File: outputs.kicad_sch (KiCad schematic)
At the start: 38 parts, among them IC1 TLE9201SG, Q1 ISL9V3040D3ST, Q2 ISL9V3040D3ST, Q3 DMN6040SK3-13, Q4 DMN6040SK3-13, U2 VNLD5160TR-E, U3 VNLD5160TR-E, U4 VNLD5160TR-E, U7 VNLD5160TR-E, U8 VNLD5160TR-E

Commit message: ACR mosfet
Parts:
- removed U3: VNLD5160TR-E, VNLD5160TR-E:SO_160TR-E_STM, symbol VNLD5160TR-E:VNLD5160TR-E
- added Q5: BUK9K52-60E,115, BUK9K52-60E:BUK7K6R840E115, symbol BUK9K52-60E_115:BUK9K52-60E,115
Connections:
- net ACR_1: now also Q5.7 (D1_1), Q5.8 (D1_2), Q5.9 (D1_3)
- net ACR_2: now also Q5.10 (D2_3), Q5.5 (D2_1), Q5.6 (D2_2); no longer U2.6 (DRAIN2)
- net GND: now also Q5.1 (S1), Q5.3 (S2)
- net INJ_1: now also U2.8 (DRAIN1)
- net INJ_2: now also U2.6 (DRAIN2); no longer U2.8 (DRAIN1)
- net MCU_ACR1: now also Q5.2 (G1)
- net MCU_ACR2: now also Q5.4 (G2); no longer U2.3 (IN2/VSUPPLY2)
- net MCU_INJ1: now also R3.1, U2.1 (IN1/VSUPPLY1); no longer R6.1
- net MCU_INJ2: now also R6.1, U2.3 (IN2/VSUPPLY2); no longer R3.1, U2.1 (IN1/VSUPPLY1)
- no-connect marks 11 -> 9
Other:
- note added: "ACR"
- note added: "ACR use same as Harley BUK9K52-60E"
- note added: "CCFC: Harley uses 2N06L35 TODO!"
- note added: "INJECTORS"
- note removed: "INJECTORS & ACR"

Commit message: some documentation and etc_dir added
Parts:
- R14: value R_Small -> 4.7K
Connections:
- net ETC_DIS: now reaches IC1.11 (DIS), R14.1
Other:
- note added: "COOLANT FAN PULLS AROUND 4A WHEN CONSTANT 100%, INITIALLY PULLING UP TO 8A FOR GETTING SPINNING HARLEY USES: HUFA76429D3 POSSIBLE: https://www.digikey.de/de/products/detail/onsemi/HUF76629D3ST/4553106 AND: https://www.digikey.de/de/products/detail/diodes-incorporated/DMN6040SK3-13/8545933 Weytronik: https://www.digikey.de/de/products/detail/vishay-siliconix/SISS54DN-T1-GE3/14004251?s=N4IgTCBcDaIM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"
- note added: "H2OS Heaters are PWM Controlled and max out at about 0.9 Amps at room temperature, then reducing with heat coming. VNLD5160TR-E should work. Will test"
- note added: "Harley Uses: https://www.mouser.de/ProductDetail/onsemi/FGB3040G2-F085C?qs=2WXlatMagcHzMRj1hscbYQ%3D%3D ISL9V3040D3ST should work though"
- note added: "INJECTORS MEASURED TO TAKE MAX 1A EACH WHEN OPEN VNLD5160TR-E should be fine"
- note added: "TODO: PURGE AND VVT SOLENOIDS NOT MEASURED YET AT ALL"
- note removed: "COOLANT FAN PULLS AROUND 4A WHEN CONSTANT 100%, INITIALLY PULLING UP TO 8A FOR GETTING SPINNING HARLEY USES: HUFA76429D3 POSSIBLE: https://www.digikey.de/de/products/detail/onsemi/HUF76629D3ST/4553106 AND: https://www.digikey.de/de/products/detail/diodes-incorporated/DMN6040SK3-13/8545933"
- note removed: "H2OS Heaters are PWM Controlled and max out at about 0.9 Amps at room temperature, then reducing with coming heat"
- note removed: "Harley Uses: https://www.mouser.de/ProductDetail/onsemi/FGB3040G2-F085C?qs=2WXlatMagcHzMRj1hscbYQ%3D%3D"
- note removed: "INJECTORS MEASURED TO TAKE MAX 1A EACH WHEN OPEN"
- moved on the sheet: C10, C11, C12, C13, C14, C15, C16, C17, C5, C6, C7, C8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

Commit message: update main connector footprint
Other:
- note added: "H2OS Heaters are PWM Controlled and max out at about 0.9 Amps at room temperature, then reducing with heat coming. VNLD5160TR-E should work. Will test HD uses https://www.vishay.com/docs/71506/sq4946aey.pdf"
- note added: "INJECTORS MEASURED TO TAKE MAX 1A EACH WHEN OPEN VNLD5160TR-E should be fine HARLEY uses 2N06L35"
- note removed: "H2OS Heaters are PWM Controlled and max out at about 0.9 Amps at room temperature, then reducing with heat coming. VNLD5160TR-E should work. Will test"
- note removed: "INJECTORS MEASURED TO TAKE MAX 1A EACH WHEN OPEN VNLD5160TR-E should be fine"
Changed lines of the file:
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@@
 			(font
 				(size 2 2)
-				(thickness 0.6)
-				(bold yes)
+				(thickness 0.25)
 				(color 43 255 15 1)
 			)
@@
 		)
 	)
-	(text "INJECTORS MEASURED TO TAKE MAX 1A EACH WHEN OPEN\nVNLD5160TR-E should be fine"
+	(text "INJECTORS MEASURED TO TAKE MAX 1A EACH WHEN OPEN\nVNLD5160TR-E should be fine\nHARLEY uses 2N06L35"
 		(exclude_from_sim no)
 		(at 103.124 61.722 0)
@@
 		)
 	)
-	(text "H2OS Heaters are PWM Controlled and max out at about 0.9 Amps\nat room temperature, then reducing with heat coming.\nVNLD5160TR-E should work. Will test"
+	(text "H2OS Heaters are PWM Controlled and max out at about 0.9 Amps\nat room temperature, then reducing with heat coming.\nVNLD5160TR-E should work. Will test\nHD uses https://www.vishay.com/docs/71506/sq4946aey.pdf"
 		(exclude_from_sim no)
 		(at 306.578 156.21 0)
@@
 				(thickness 0.6)
 				(bold yes)
+				(color 255 238 0 1)
+			)
+		)
+	)
+	(text "Harley Uses:\nhttps://www.mouser.de/ProductDetail/onsemi/FGB3040G2-F085C?qs=2WXlatMagcHzMRj1hscbYQ%3D%3D\nISL9V3040D3ST should work though"
+		(exclude_from_sim no)
+		(at 98.806 278.13 0)
+		(effects
+			(font
+				(size 2 2)
+				(thickness 0.25)
 				(color 43 255 15 1)
 			)
@@
 			(font
 				(size 2 2)
-				(thickness 0.6)
-				(bold yes)
+				(thickness 0.25)
 				(color 43 255 15 1)
 			)
@@
 	(text "CCFC & HO2HTR"
 		(exclude_from_sim no)
-		(at 307.34 217.424 0)
+		(at 308.102 219.71 0)
 		(effects
 			(font
@@
 	(text "H2OS Heaters"
 		(exclude_from_sim no)
-		(at 308.61 167.894 0)
+		(at 307.34 171.704 0)
 		(effects
 			(font
@@
 	(text "CCFC: Harley uses 2N06L35 TODO!"
 		(exclude_from_sim no)
-		(at 306.07 210.82 0)
+		(at 306.832 213.106 0)
 		(effects
 			(font
@@
 				(thickness 0.6)
 				(bold yes)
-				(color 43 255 15 1)
+				(color 255 238 0 1)
 			)
 		)

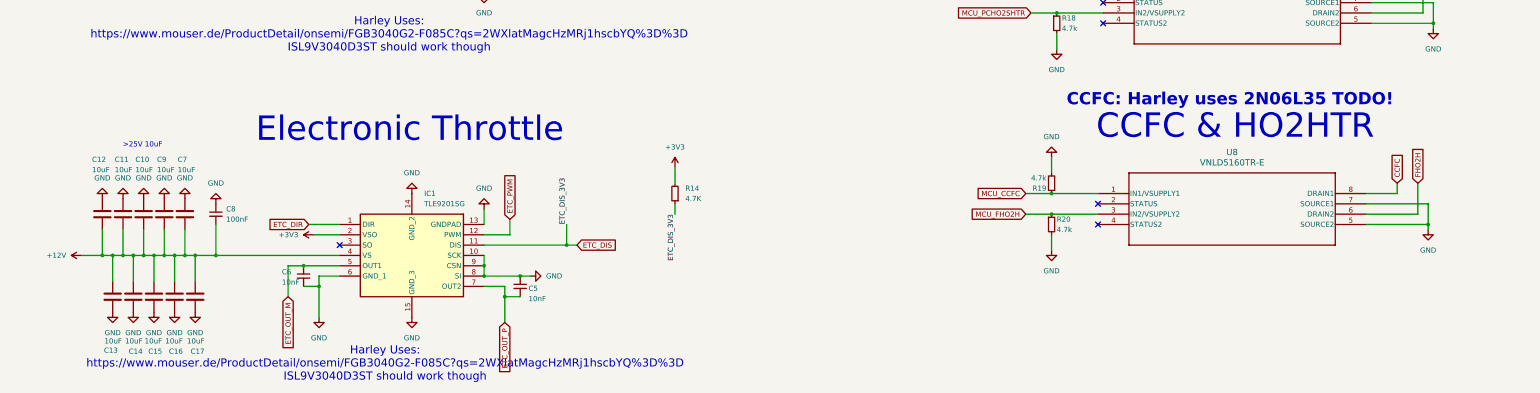
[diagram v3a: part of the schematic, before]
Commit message: ccfc mosfet and power changes
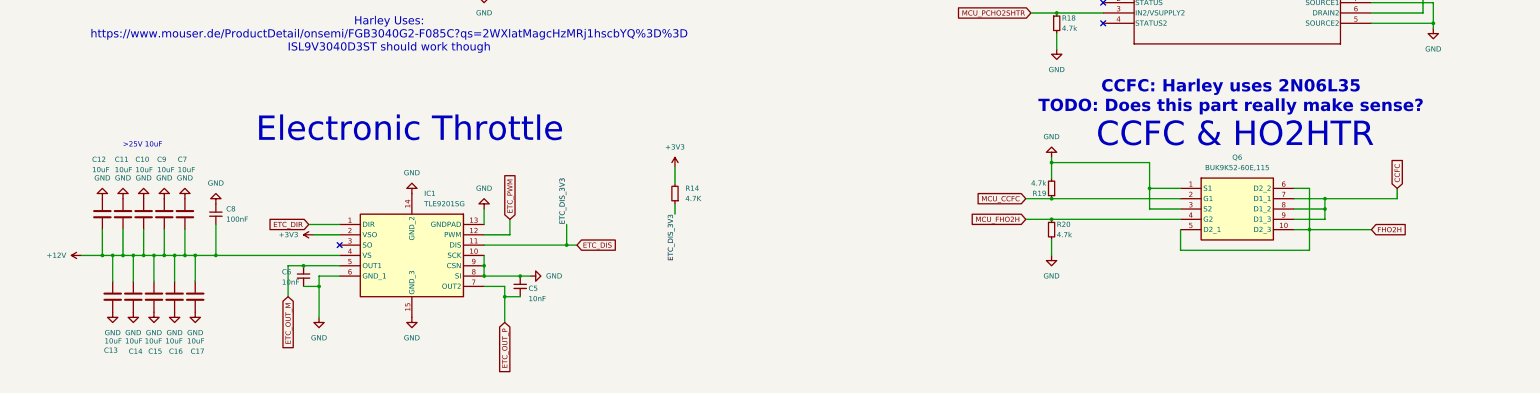
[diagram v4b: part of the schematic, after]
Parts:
- removed U8: VNLD5160TR-E, VNLD5160TR-E:SO_160TR-E_STM, symbol VNLD5160TR-E:VNLD5160TR-E
- added Q6: BUK9K52-60E,115, BUK9K52-60E:BUK7K6R840E115, symbol BUK9K52-60E_115:BUK9K52-60E,115
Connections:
- net CCFC: now also Q6.7 (D1_1), Q6.8 (D1_2), Q6.9 (D1_3)
- net FHO2H: now also Q6.10 (D2_3), Q6.5 (D2_1), Q6.6 (D2_2)
- net GND: now also Q6.1 (S1), Q6.3 (S2)
- net MCU_CCFC: now also Q6.2 (G1)
- net MCU_FHO2H: now also Q6.4 (G2)
- no-connect marks 9 -> 7
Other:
- note added: "CCFC: Harley uses 2N06L35 TODO: Does this part really make sense?"
- note removed: "CCFC: Harley uses 2N06L35 TODO!"
- moved on the sheet: R19, R20
